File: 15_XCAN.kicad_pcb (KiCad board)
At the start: 2 copper layers, 20.3 x 20.3 mm, 16 parts, among them J1 Conn_01x01, J2 Conn_01x01, J3 Conn_01x01, J4 Conn_01x01, J5 Conn_01x01, J6 Conn_01x01, J7 Conn_01x01, U1 MCP2551-I-SN

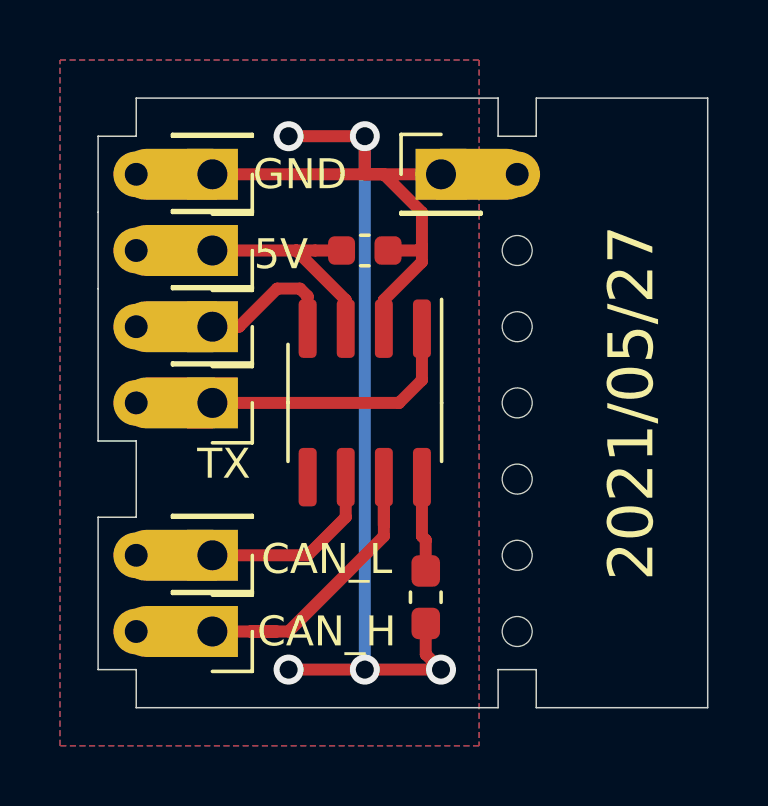
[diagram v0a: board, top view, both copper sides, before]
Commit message: réduction de taille du pcb
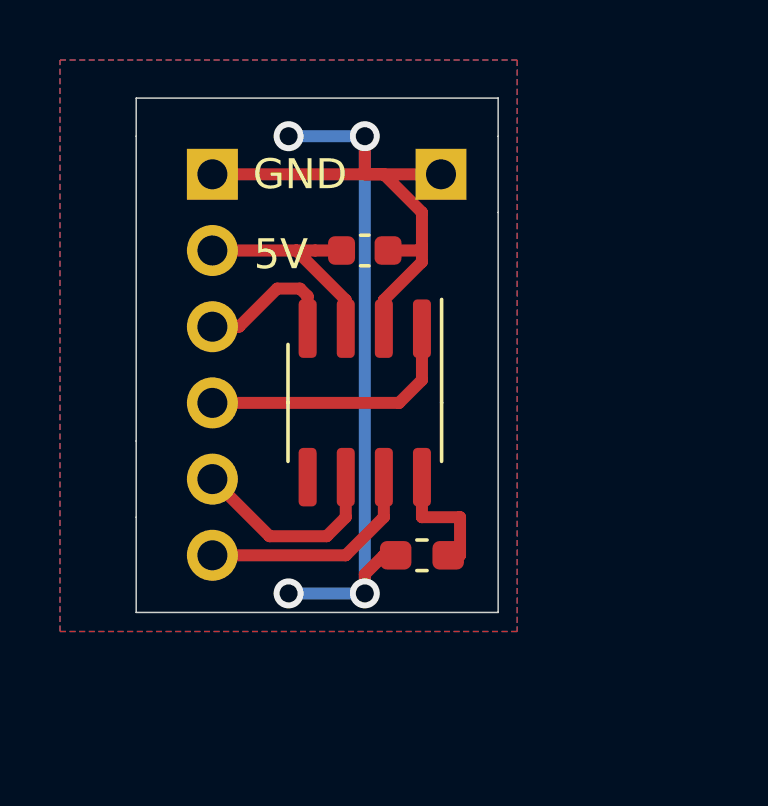
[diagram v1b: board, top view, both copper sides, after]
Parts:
- removed H1, H2, H3, H4, H5, H6: percage, Chimere_comps:trou
- removed J2, J3, J4, J5, J6: Conn_01x01, Chimere_mods:Castellated_conn
- J1: value Conn_01x01 -> Conn_01x06; footprint Chimere_mods:Castellated_conn -> Connector_PinHeader_2.54mm:PinHeader_1x06_P2.54mm_Vertical; moved to B.Cu
- J7: footprint Chimere_mods:Castellated_conn -> Connector_PinHeader_2.54mm:PinHeader_1x01_P2.54mm_Vertical; moved to B.Cu
- moved R1 1.40 mm to (111.1, 76.2), turned to 0 degrees
- turned J7 to 180 degrees
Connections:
- U1 pad 5: Net-(U1-Pad5) -> unconnected-(U1-Pad5)
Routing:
- net GND: track 44.1 -> 39.2 mm, vias 5 -> 4
- net CAN_H: track 11.5 -> 7.58 mm
- net Net-(R1-Pad2): track 3.18 -> 4.27 mm
- net CAN_L: track 6.31 -> 6.83 mm
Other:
- board size 20.3 x 20.3 mm -> 12.1 x 17.1 mm
- board text removed: "2021/05/27"
- board text removed: "github.com/ ThierryOrlandi/ 15_XCAN"
